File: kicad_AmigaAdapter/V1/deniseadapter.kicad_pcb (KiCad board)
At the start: 2 copper layers, 26.7 x 62.2 mm, 14 parts, among them U1 74LVC86, U2 74LVC574, U3 74LVC574, U4 TLV74333PDBVR

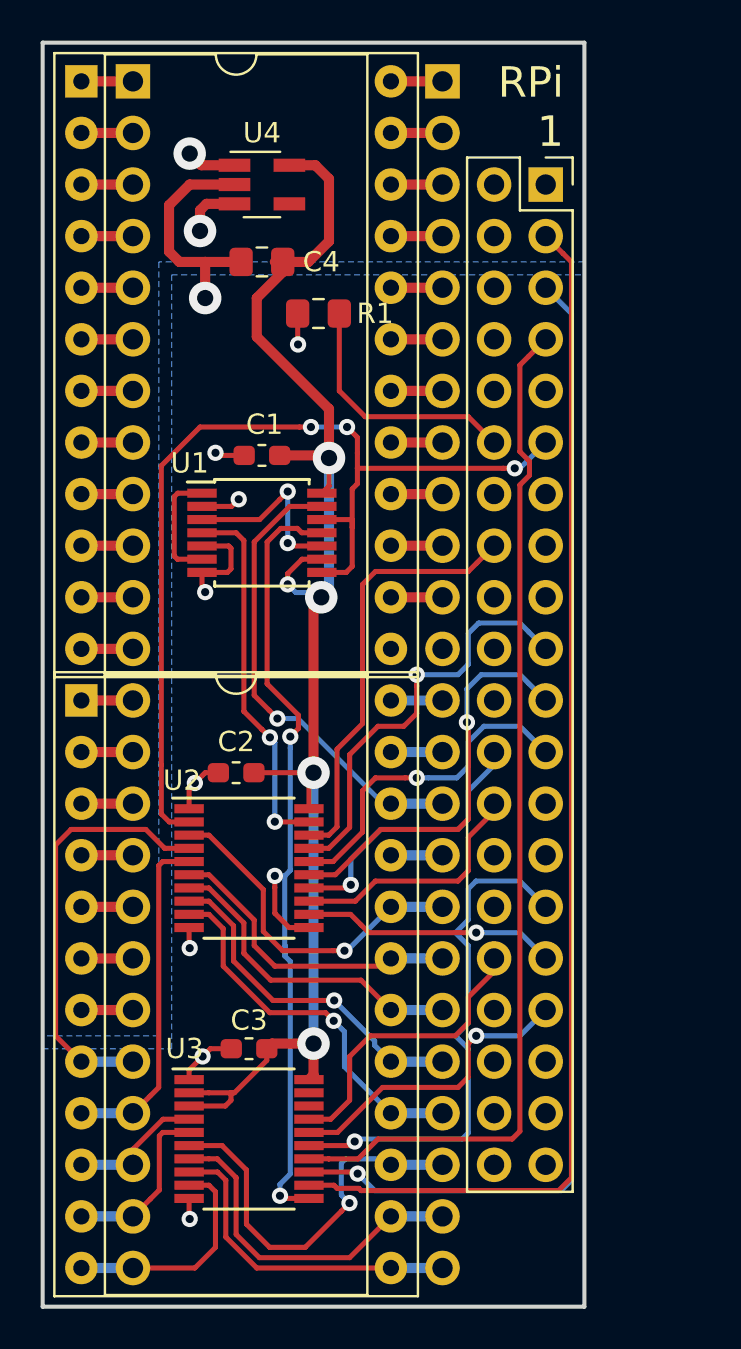
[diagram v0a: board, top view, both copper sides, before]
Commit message: Add switch connector and slightly re-arrange xor gates
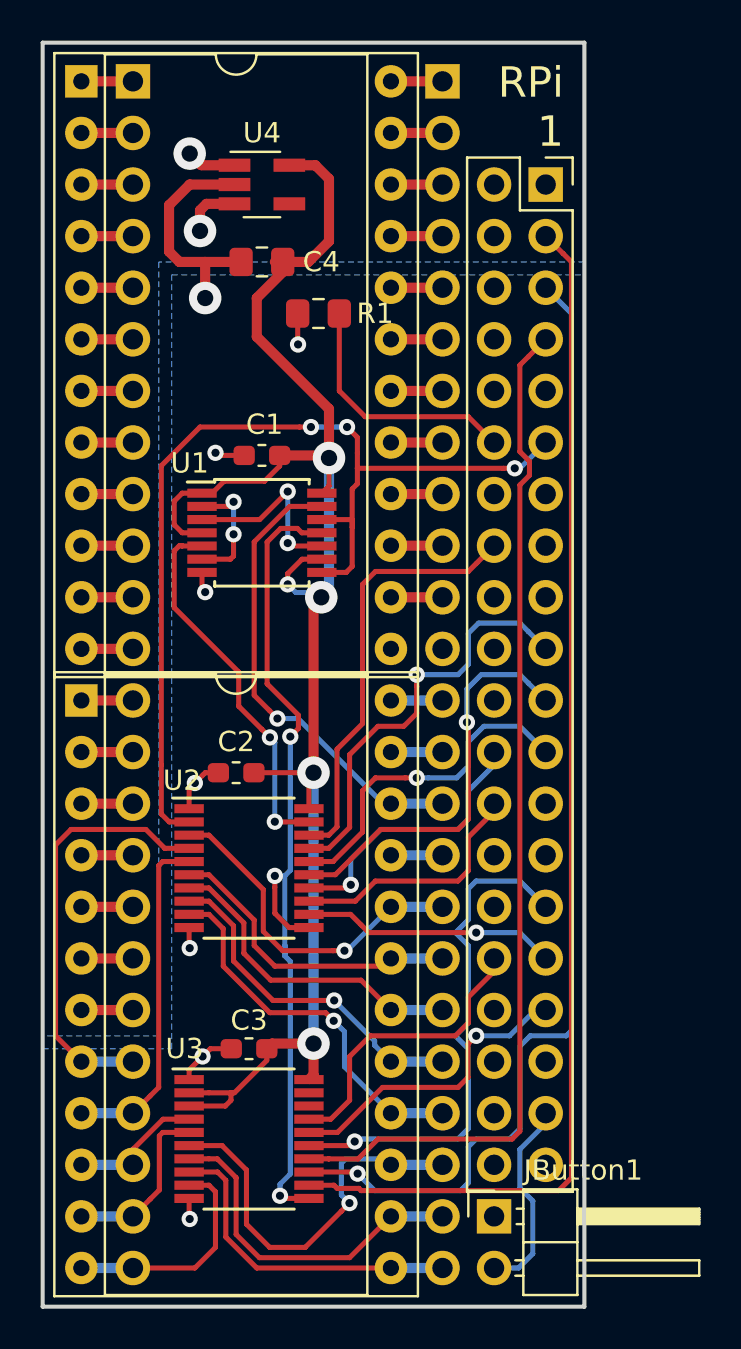
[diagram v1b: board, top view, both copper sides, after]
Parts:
- added JButton1: Conn_01x02, Connector_PinHeader_2.54mm:PinHeader_1x02_P2.54mm_Horizontal, F.Cu at (137.2, 116.8)
- R1: value 1K -> 3k3
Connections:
- U1 pad 1: Net-(U1-Pad1) -> +3V3
- U1 pad 2: GND -> Net-(U1-Pad2)
- U1 pad 4: Net-(U1-Pad4) -> +3V3
- U1 pad 5: GND -> Net-(U1-Pad5)
- U1 pad 6: Net-(U1-Pad1) -> Net-(U1-Pad2)
- U2 pad 19: Net-(U1-Pad4) -> Net-(U1-Pad5)
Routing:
- net Net-(U1-Pad5): track 0.00 -> 18.6 mm, vias 0 -> 2
- net Net-(U1-Pad4): track 18.4 -> 0.00 mm, vias 2 -> 0
- net Net-(JButton1-Pad2): track 0.00 -> 9.90 mm
- net +3V3: track 75.5 -> 84.6 mm
- net GND: track 29.1 -> 23.2 mm, vias 9 -> 8
- net Net-(U1-Pad2): track 0.00 -> 5.93 mm, vias 0 -> 2
- net Net-(U1-Pad1): track 5.79 -> 0.00 mm
- net /PiB1: track 58.0 -> 57.1 mm

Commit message: User GPIO 16 for the button. Create gerber files.
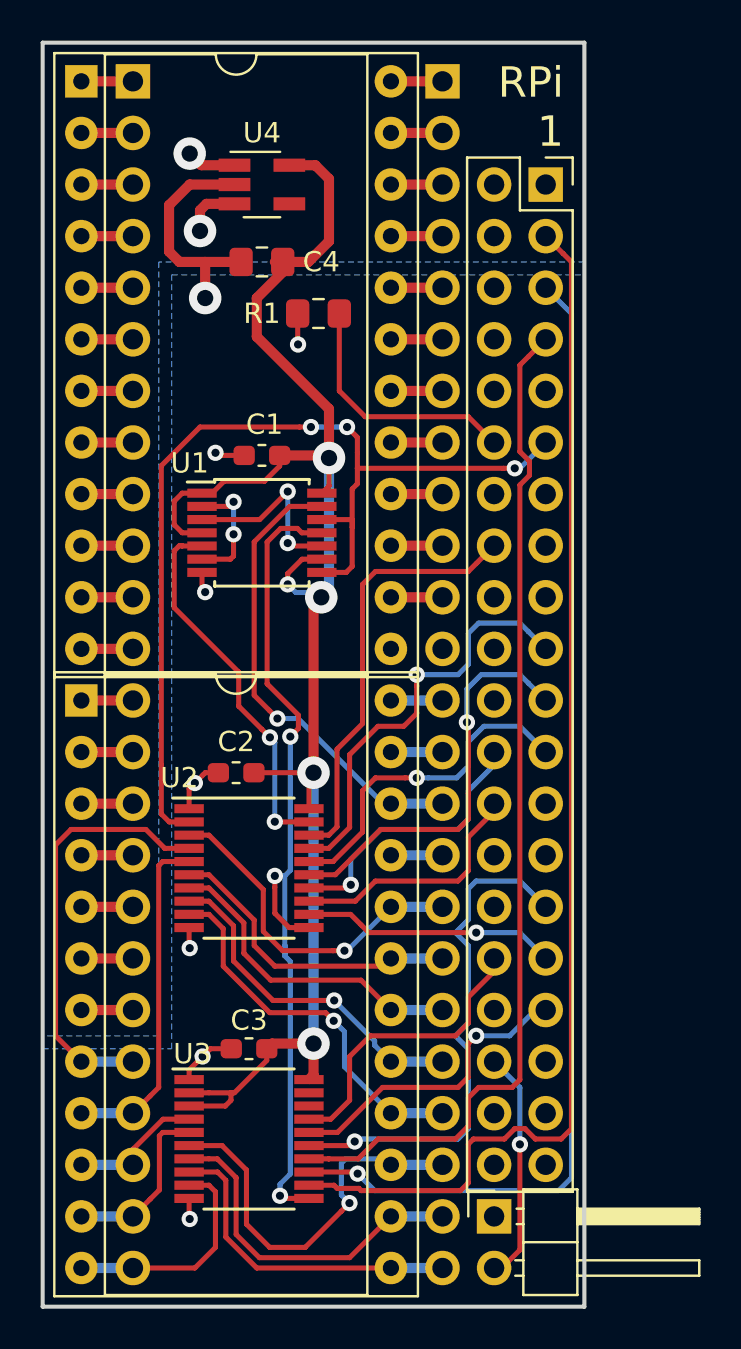
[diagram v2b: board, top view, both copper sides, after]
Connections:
- JRaspberryPiZero1 pad 36: Net-(JRaspberryPiZero1-Pad36) -> Net-(JButton1-Pad2)
- JRaspberryPiZero1 pad 37: Net-(JButton1-Pad2) -> Net-(JRaspberryPiZero1-Pad37)
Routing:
- net Net-(JButton1-Pad2): track 9.90 -> 11.4 mm, vias 0 -> 1
- net /PiB1: track 57.1 -> 57.9 mm
- net /PiB2: track 50.9 -> 50.2 mm
